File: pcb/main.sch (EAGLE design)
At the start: 23 parts, among them Q1 MOSFET-NCHANNEL2N7000

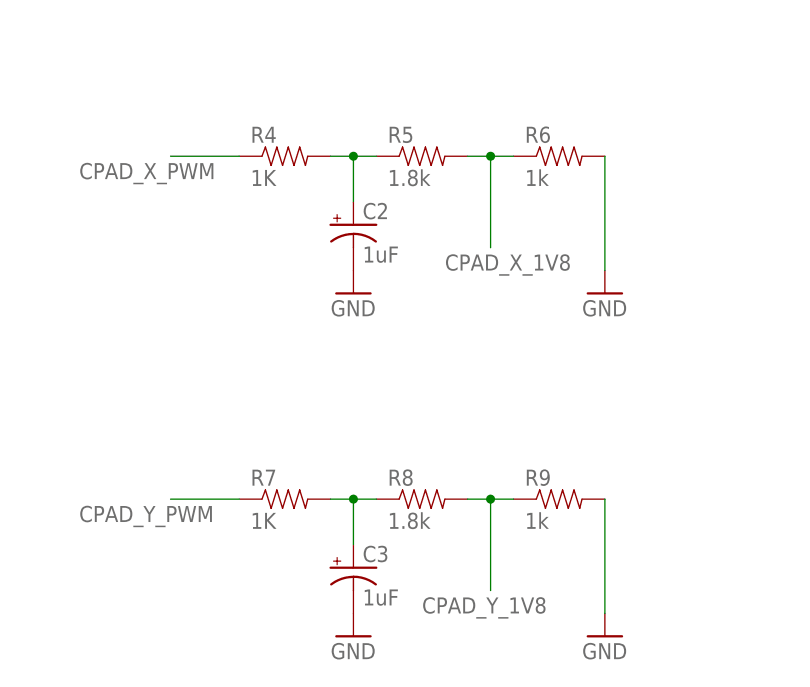
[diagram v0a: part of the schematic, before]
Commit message: updated low pass filter
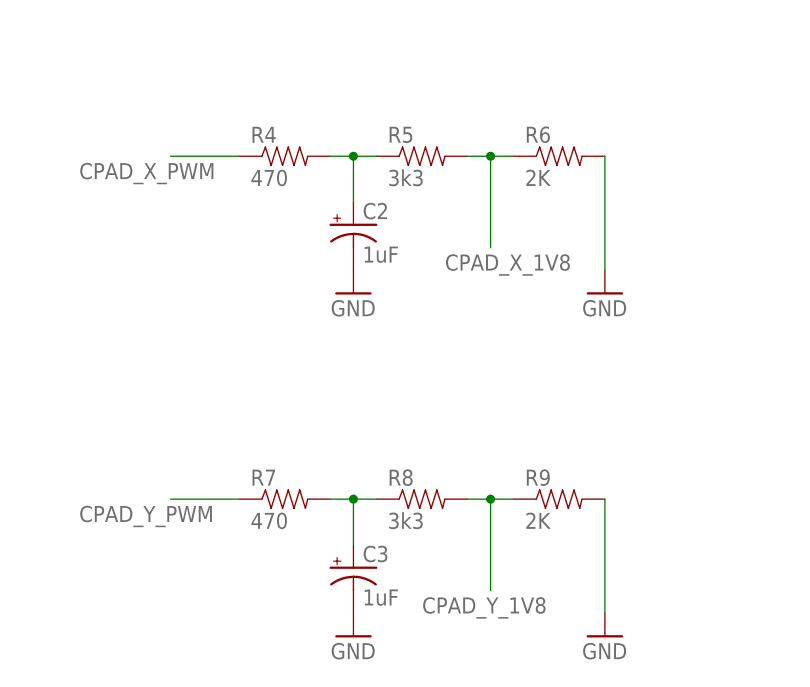
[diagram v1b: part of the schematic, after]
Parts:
- R4, R7: value 1K -> 470
- R5, R8: value 1.8k -> 3k3
- R6, R9: value 1k -> 2K
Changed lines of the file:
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@@
 <?xml version="1.0" encoding="utf-8"?>
 <!DOCTYPE eagle SYSTEM "eagle.dtd">
-<eagle version="6.5.0">
+<eagle version="7.1.0">
 <drawing>
 <settings>
@@
 <part name="SUPPLY3" library="SparkFun-Aesthetics" deviceset="5V" device=""/>
 <part name="SUPPLY4" library="SparkFun-Aesthetics" deviceset="3.3V" device=""/>
-<part name="R4" library="SparkFun-Resistors" deviceset="RESISTOR" device="PTH-1/4W" value="1K"/>
+<part name="R4" library="SparkFun-Resistors" deviceset="RESISTOR" device="PTH-1/4W" value="470"/>
 <part name="C2" library="SparkFun-Capacitors" deviceset="CAP_POL" device="PTH2" value="1uF"/>
-<part name="R5" library="SparkFun-Resistors" deviceset="RESISTOR" device="PTH-1/4W" value="1.8k"/>
-<part name="R6" library="SparkFun-Resistors" deviceset="RESISTOR" device="PTH-1/4W" value="1k"/>
+<part name="R5" library="SparkFun-Resistors" deviceset="RESISTOR" device="PTH-1/4W" value="3k3"/>
+<part name="R6" library="SparkFun-Resistors" deviceset="RESISTOR" device="PTH-1/4W" value="2K"/>
 <part name="GND4" library="SparkFun-Aesthetics" deviceset="GND" device=""/>
 <part name="GND5" library="SparkFun-Aesthetics" deviceset="GND" device=""/>
-<part name="R7" library="SparkFun-Resistors" deviceset="RESISTOR" device="PTH-1/4W" value="1K"/>
+<part name="R7" library="SparkFun-Resistors" deviceset="RESISTOR" device="PTH-1/4W" value="470"/>
 <part name="C3" library="SparkFun-Capacitors" deviceset="CAP_POL" device="PTH2" value="1uF"/>
-<part name="R8" library="SparkFun-Resistors" deviceset="RESISTOR" device="PTH-1/4W" value="1.8k"/>
-<part name="R9" library="SparkFun-Resistors" deviceset="RESISTOR" device="PTH-1/4W" value="1k"/>
+<part name="R8" library="SparkFun-Resistors" deviceset="RESISTOR" device="PTH-1/4W" value="3k3"/>
+<part name="R9" library="SparkFun-Resistors" deviceset="RESISTOR" device="PTH-1/4W" value="2K"/>
 <part name="GND6" library="SparkFun-Aesthetics" deviceset="GND" device=""/>
 <part name="GND7" library="SparkFun-Aesthetics" deviceset="GND" device=""/>
